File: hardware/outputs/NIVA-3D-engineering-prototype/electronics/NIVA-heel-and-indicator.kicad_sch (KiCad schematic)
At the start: 15 parts, among them U4 MCP6001T-I/OT

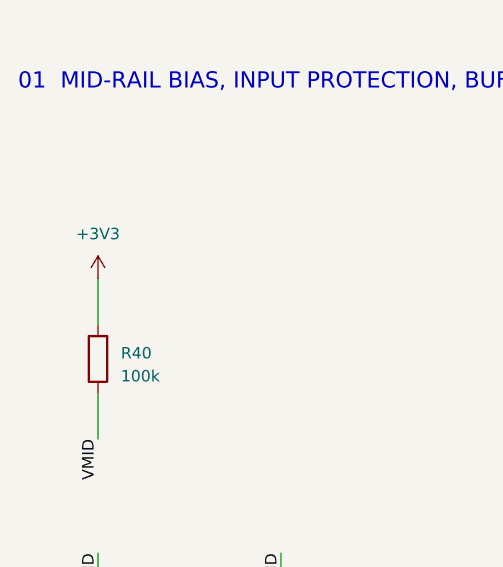
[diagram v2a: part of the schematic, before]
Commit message: Add cartridge interconnect PCB, charging dock PCB and dock enclosure; ratiometric ADC reference
- Pod schematic: MCP3208 VREF driven from VEXC (the sensor excitation rail) so every
  channel is ratiometric in hardware; CH6 reads +3V3/2 as a rail monitor.
- Cartridge: 3.4 mm interconnect strip (cell leads, polyfuse, lid-plate leads, underside
  dock pads), hand-routed; ERC/DRC clean with schematic parity.
- Dock: USB-C sink, MCP73831 charger gated by an LM393 NTC window comparator, spring
  pins to the cartridge pads; autorouted (Freerouting) and DRC clean.
- Fabrication data for both boards written only as review-only sets with open blockers.
- Dock enclosure (base, top with keyed well, tab ledge, snap latch, light pipe) generated
  from niva_layout.py; interference audit reports only the expected spring-pin contacts.
- Shared CAD helpers and cartridge builders moved to niva_cad_lib.py.

Co-Authored-By: Claude Opus 5.5 <noreply@anthropic.com>
Claude-Session: https://claude.ai/code/session_01HNzeJFE5uNHjapog53SHnm
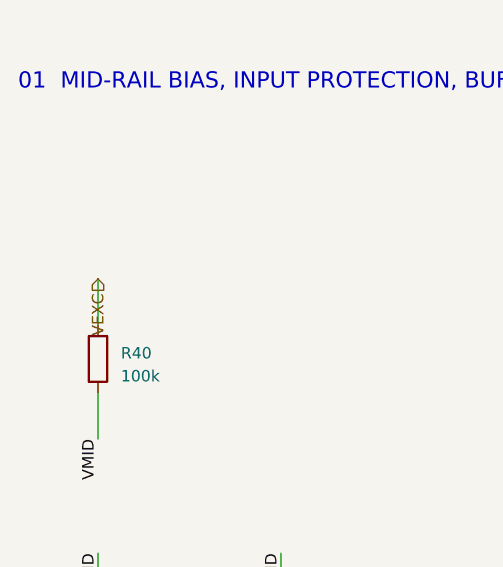
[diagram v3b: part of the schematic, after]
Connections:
- net +3V3: no longer R40.1
- new net VEXC: R40.1

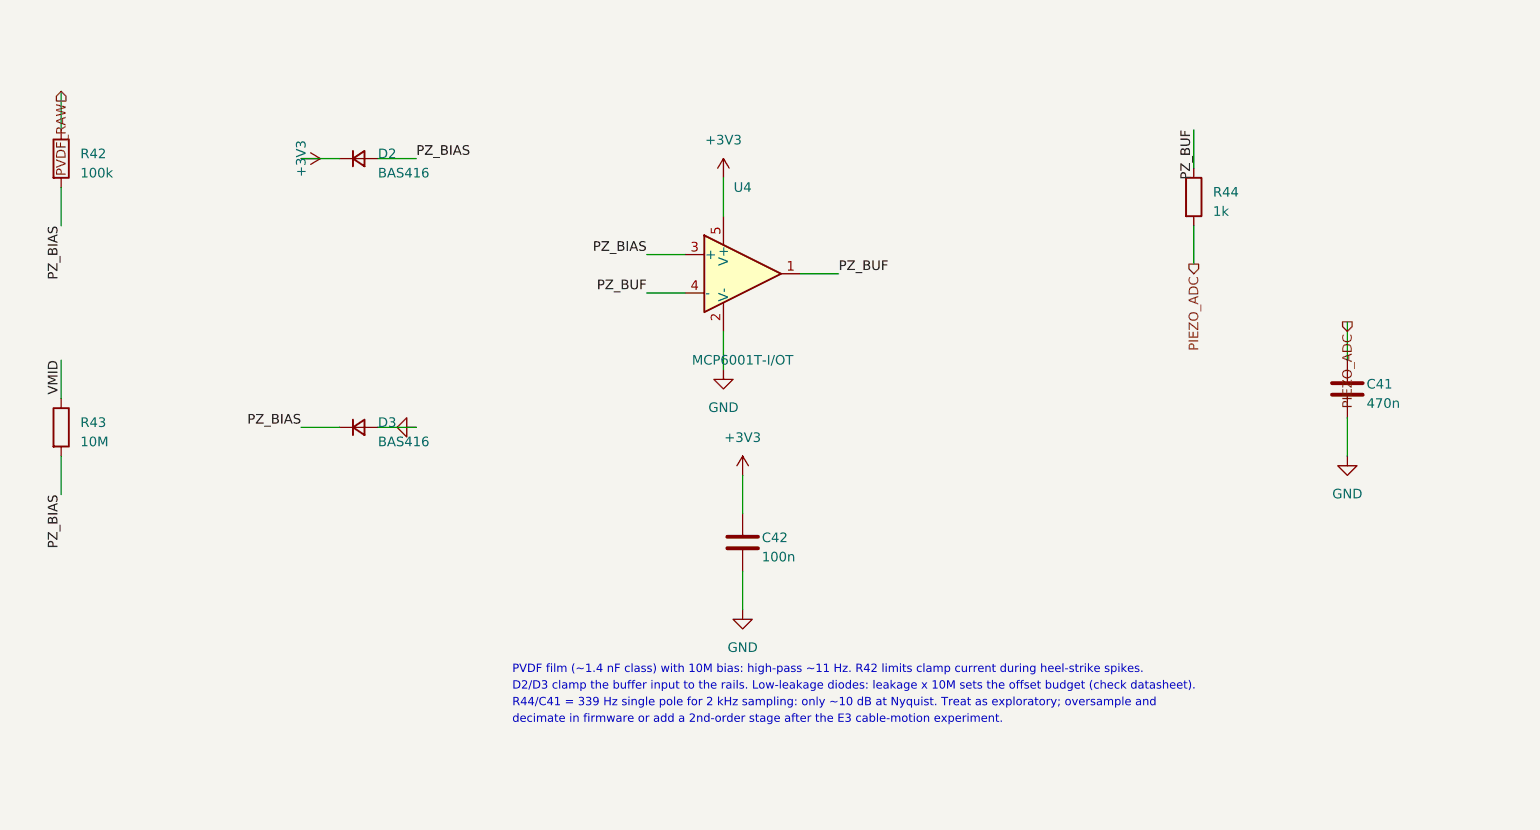
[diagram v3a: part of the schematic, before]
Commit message: Route the pod PCB, add BAV199 clamp, insole sensing flex, verification plan
- Pod: 0.15/0.127 mm rules; every GND pad fanned out to the In1 plane before
  autorouting, signals routed with Freerouting, GND pours stitched on all layers.
  KiCad DRC: 0 errors, 0 unconnected, schematic parity clean.
- D2/D3 BAS416 singles replaced by one BAV199 series pair on a project symbol
  that states the datasheet pinning.
- Insole flex (right/left medium): five interdigitated shunt-mode electrodes,
  PVDF bond pads, paired lanes to the heel tab, above-collar transition with the
  insert ID resistor; F.Cu only and no parts underfoot. ERC/DRC clean.
- export_niva_electronics.py writes all board outputs; fabrication data only in
  per-board fab-REVIEW-ONLY-NOT-RELEASED folders with open blockers.
- VERIFICATION-PLAN.md: sealing, skin-contact and cleaning test plan (no claims).
- Dock CAD re-audited against the new dock STEP; pod CAD against the routed PCBA.
- Blender import linearises KiCad GLB colours; dock and insole-flex scenes added.
- README, ELECTRICAL-REVIEW and PRINT-AND-ASSEMBLY updated for Rev C.1.

Co-Authored-By: Claude Opus 5.5 <noreply@anthropic.com>
Claude-Session: https://claude.ai/code/session_01HNzeJFE5uNHjapog53SHnm
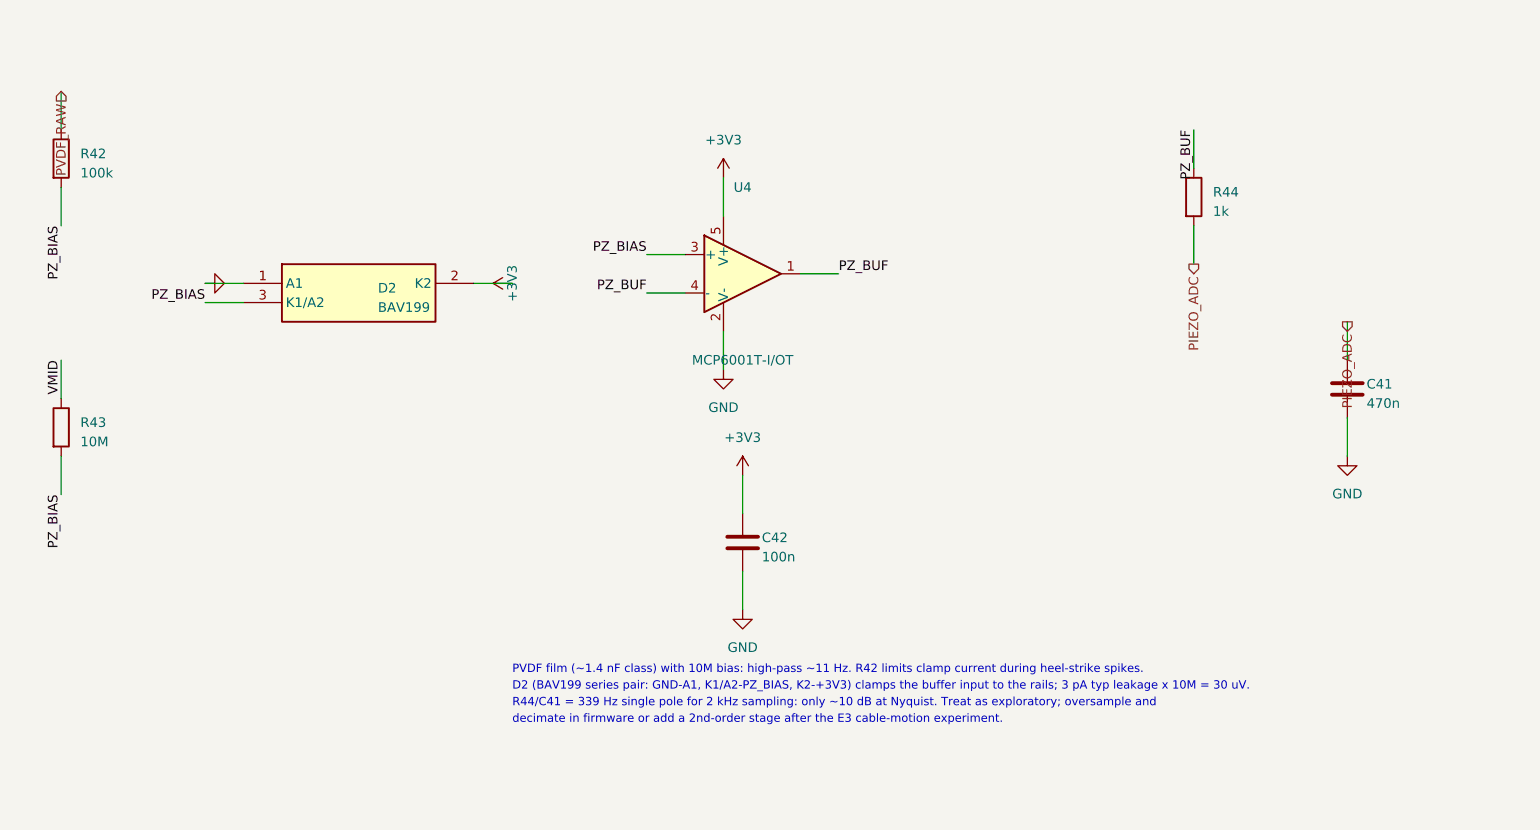
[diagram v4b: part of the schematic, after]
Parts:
- removed D3: BAS416, Diode_SMD:D_SOD-323, symbol Device:D_Small
- D2: value BAS416 -> BAV199; footprint Diode_SMD:D_SOD-323 -> Package_TO_SOT_SMD:SOT-23; symbol Device:D_Small -> NIVA:BAV199; MPN BAS416 (low-leakage, SOD-323) -> BAV199,215 (Nexperia) low-leakage series pair, SOT-23
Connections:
- net +3V3: now also D2.2 (K2); no longer D2.1 (K)
- net GND: now also D2.1 (A1)
- net PZ_BIAS: now also D2.3 (K1/A2); no longer D2.2 (A)
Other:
- note added: "D2 (BAV199 series pair: GND-A1, K1/A2-PZ_BIAS, K2-+3V3) clamps the buffer input to the rails; 3 pA typ leakage x 10M = 30 uV."
- note removed: "D2/D3 clamp the buffer input to the rails. Low-leakage diodes: leakage x 10M sets the offset budget (check datasheet)."
